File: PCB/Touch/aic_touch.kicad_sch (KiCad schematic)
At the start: 14 parts, among them J1 Antenna, J2 PN5180, J3 PN532, J4 Display, U1 Pico

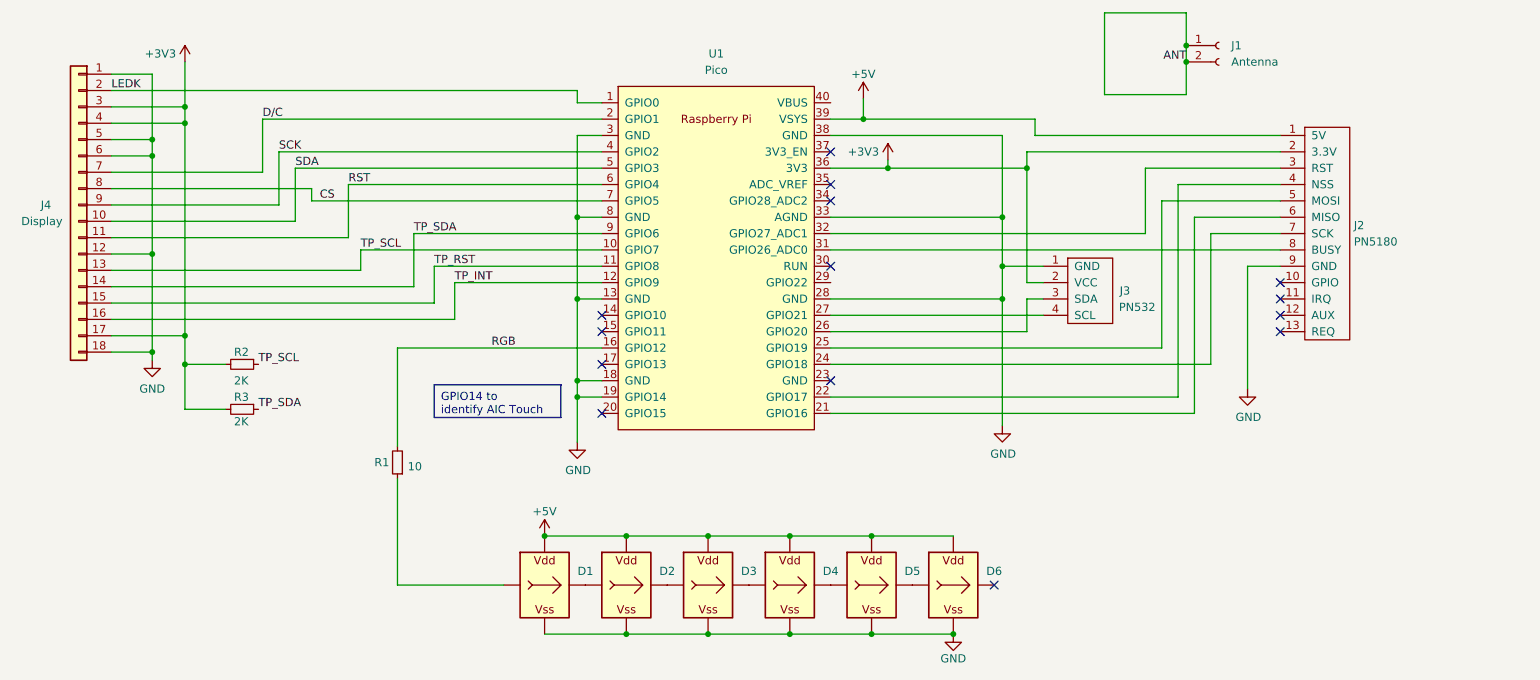
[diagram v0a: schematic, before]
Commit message: Fix PCB issue and change to 4020 RGB
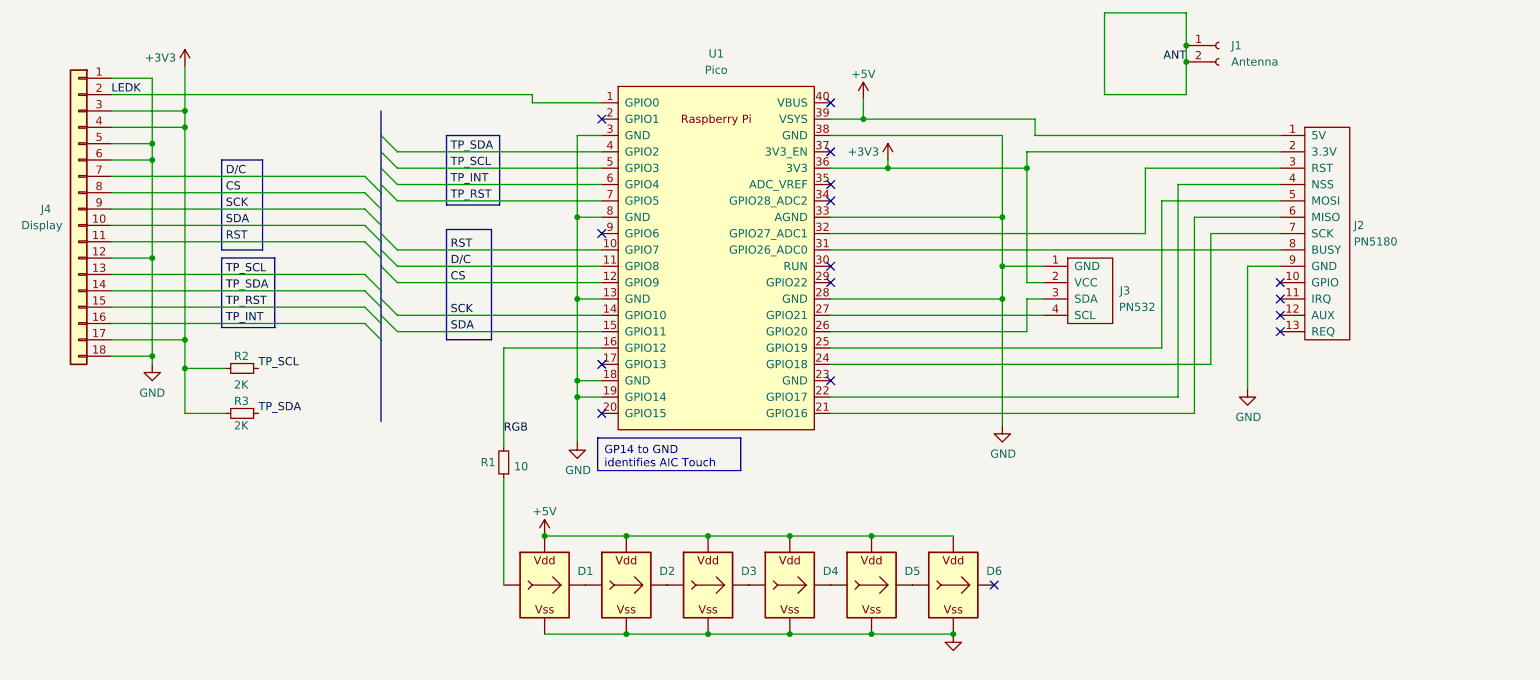
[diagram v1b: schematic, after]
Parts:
- D1, D2, D3, D4, D5, D6: footprint aic_pico:WS2812B-1204 -> aic_pico:WS2812B-4020
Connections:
- net CS: now also U1.12 (GPIO9); no longer U1.7 (GPIO5)
- net D/C: now also U1.11 (GPIO8); no longer U1.2 (GPIO1)
- net RST: now also U1.10 (GPIO7); no longer U1.6 (GPIO4)
- net SCK: now also U1.14 (GPIO10); no longer U1.4 (GPIO2)
- net SDA: now also U1.15 (GPIO11); no longer U1.5 (GPIO3)
- net TP_INT: now also U1.6 (GPIO4); no longer U1.12 (GPIO9)
- net TP_RST: now also U1.7 (GPIO5); no longer U1.11 (GPIO8)
- net TP_SCL: now also U1.5 (GPIO3); no longer U1.10 (GPIO7)
- net TP_SDA: now also U1.4 (GPIO2); no longer U1.9 (GPIO6)
- no-connect marks 14 -> 16
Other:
- moved on the sheet: J4, R1, R2, R3

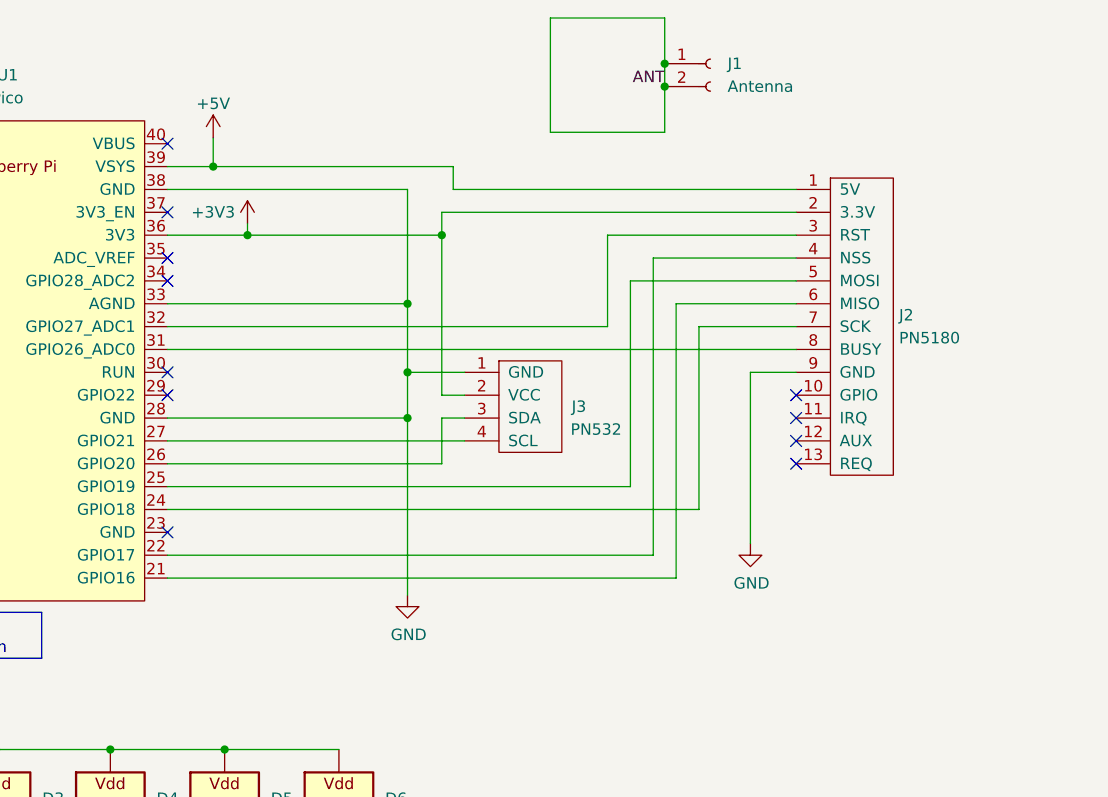
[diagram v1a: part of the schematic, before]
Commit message: Power filtering for PN5180 on AIC touch
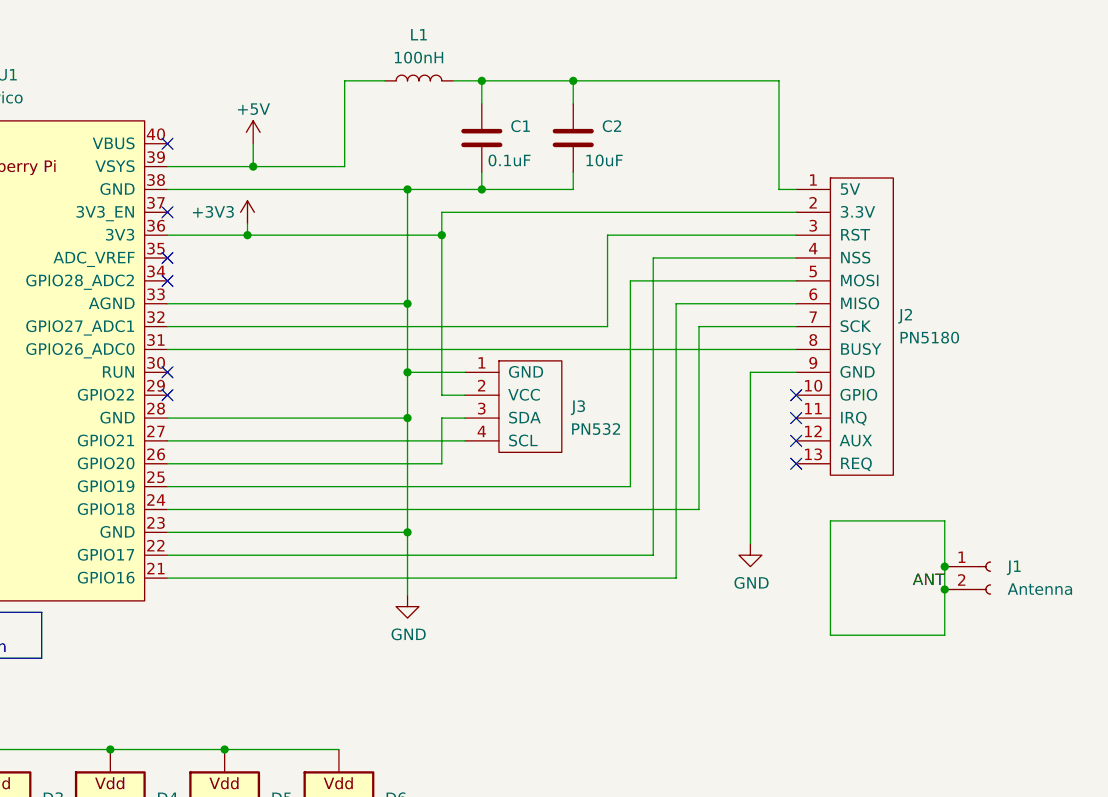
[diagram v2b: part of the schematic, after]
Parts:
- added C1: 0.1uF, Capacitor_SMD:C_0603_1608Metric, symbol Device:C
- added C2: 10uF, Capacitor_SMD:C_0603_1608Metric, symbol Device:C
- added L1: 100nH, Inductor_SMD:L_0805_2012Metric, symbol Device:L
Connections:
- net +5V: now also L1.1; no longer J2.1 (5V)
- net GND: now also U1.23 (GND), C1.2, C2.2
- new net: C1.1, C2.1, J2.1 (5V), L1.2
- no-connect marks 16 -> 15
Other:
- moved on the sheet: J1

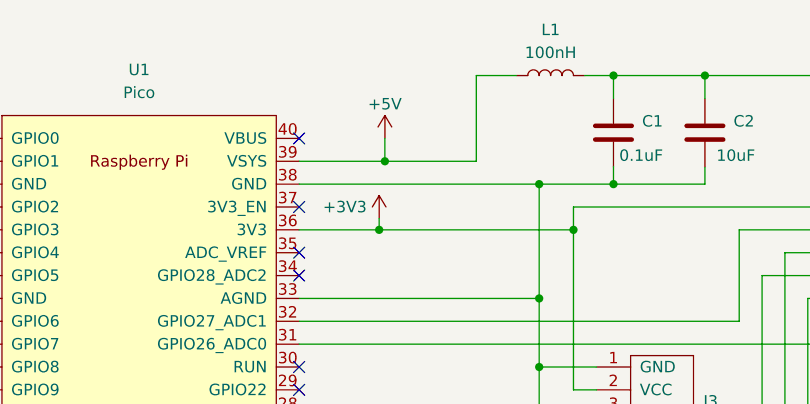
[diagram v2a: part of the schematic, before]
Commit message: L1 to 1206 and power from VBUS
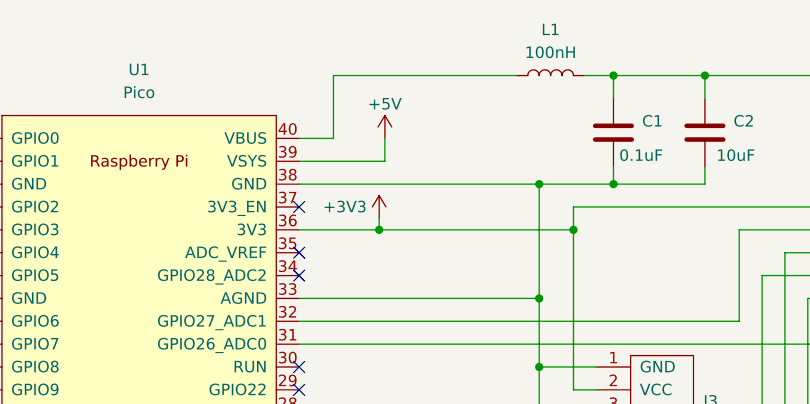
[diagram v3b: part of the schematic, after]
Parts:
- L1: footprint Inductor_SMD:L_0805_2012Metric -> Inductor_SMD:L_1206_3216Metric
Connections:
- net +5V: no longer L1.1
- net at U1.40 (VBUS): now also L1.1
- no-connect marks 15 -> 14
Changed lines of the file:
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@@
   (junction (at 236.22 93.98) (diameter 0) (color 0 0 0 0)
-  )
-  (junction (at 219.075 78.74) (diameter 0) (color 0 0 0 0)
   )
   (junction (at 295.91 125.73) (diameter 0) (color 0 0 0 0)
@@
   (no_connect (at 209.55 91.44))
   (no_connect (at 234.95 151.13))
-  (no_connect (at 209.55 76.2))
   (no_connect (at 173.99 116.84))
   (no_connect (at 279.4 104.14))
@@
     (stroke (width 0) (type default))
   )
+  (wire (pts (xy 213.36 76.2) (xy 213.36 69.215))
+    (stroke (width 0) (type default))
+  )
   (wire (pts (xy 158.75 114.3) (xy 173.99 114.3))
     (stroke (width 0) (type default))
@@
     (stroke (width 0) (type default))
   )
-  (wire (pts (xy 229.235 69.215) (xy 233.68 69.215))
+  (wire (pts (xy 213.36 69.215) (xy 233.68 69.215))
     (stroke (width 0) (type default))
   )
@@
     (stroke (width 0) (type default))
   )
-  (wire (pts (xy 219.075 78.74) (xy 229.235 78.74))
-    (stroke (width 0) (type default))
-  )
   (wire (pts (xy 295.91 123.19) (xy 295.91 125.73))
     (stroke (width 0) (type default))
@@
     (stroke (width 0) (type default))
   )
+  (wire (pts (xy 209.55 76.2) (xy 213.36 76.2))
+    (stroke (width 0) (type default))
+  )
   (wire (pts (xy 177.8 143.51) (xy 190.5 143.51))
     (stroke (width 0) (type default))
@@
   )
   (wire (pts (xy 109.22 77.47) (xy 109.22 70.485))
-    (stroke (width 0) (type default))
-  )
-  (wire (pts (xy 229.235 78.74) (xy 229.235 69.215))
     (stroke (width 0) (type default))
   )
@@
       (effects (font (size 1.27 1.27)))
     )
-    (property "Footprint" "Inductor_SMD:L_0805_2012Metric" (at 237.49 69.215 0)
-      (effects (font (size 1.27 1.27)) hide)
-    )
+    (property "Footprint" "Inductor_SMD:L_1206_3216Metric" (at 237.49 69.215 0)
+      (effects (font (size 1.27 1.27)) hide)
+    )

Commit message: Hybrid AIC Key PCB and AIC touch RGB back to 1204
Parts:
- removed L1: 100nH, Inductor_SMD:L_1206_3216Metric, symbol Device:L
- added C3: 0.1uF, Capacitor_SMD:C_0603_1608Metric, symbol Device:C
- C2: value 10uF -> 0.1uF
- D1, D2, D3, D4, D5, D6: footprint aic_pico:WS2812B-4020 -> aic_pico:WS2812B-1204
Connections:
- net +3V3: now also C2.1, C3.1
- net +5V: now also C1.1, J2.1 (5V)
- net GND: now also C3.2
- no-connect marks 14 -> 15
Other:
- moved on the sheet: C1

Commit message: Touch PCB v1.4 (may improve RF)
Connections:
- net GND: no longer J2.9 (GND), J3.1 (GND), U1.13 (GND), U1.18 (GND), U1.19 (GPIO14), U1.23 (GND), U1.28 (GND), U1.3 (GND), U1.33 (AGND), U1.8 (GND)
- new net: U1.18 (GND), U1.19 (GPIO14)
- new net 5180_GND: J2.9 (GND), U1.33 (AGND)
- new net 532_GND: J3.1 (GND), U1.13 (GND)
- no-connect marks 15 -> 18
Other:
- moved on the sheet: J2

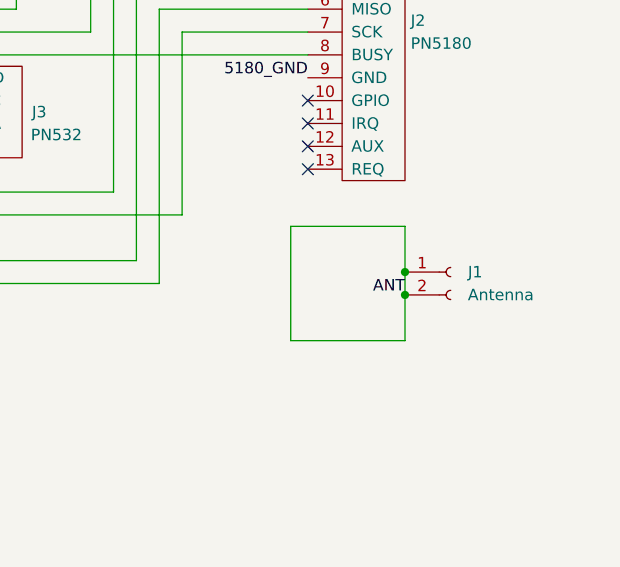
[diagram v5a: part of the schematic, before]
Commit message: Offload PN532 antenna for better signal
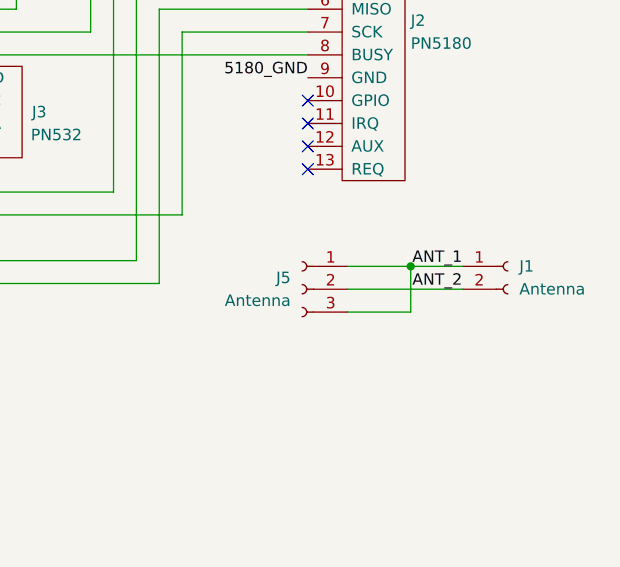
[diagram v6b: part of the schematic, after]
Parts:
- added J5: Antenna, aic_pico:ANT_3P, symbol Connector:Conn_01x03_Socket
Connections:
- net ANT renamed ANT_1
- net ANT_1: now also J5.1 (Pin_1), J5.3 (Pin_3); no longer J1.2 (Pin_2)
- new net ANT_2: J1.2 (Pin_2), J5.2 (Pin_2)
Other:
- moved on the sheet: J1
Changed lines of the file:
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@@
   (junction (at 190.5 158.75) (diameter 0) (color 0 0 0 0)
   )
+  (junction (at 296.545 122.555) (diameter 0) (color 0 0 0 0)
+  )
   (junction (at 177.8 143.51) (diameter 0) (color 0 0 0 0)
   )
@@
   (junction (at 109.22 77.47) (diameter 0) (color 0 0 0 0)
   )
-  (junction (at 295.91 123.19) (diameter 0) (color 0 0 0 0)
-  )
   (junction (at 104.14 100.33) (diameter 0) (color 0 0 0 0)
   )
@@
   )
   (junction (at 242.57 83.82) (diameter 0) (color 0 0 0 0)
-  )
-  (junction (at 295.91 125.73) (diameter 0) (color 0 0 0 0)
   )
   (junction (at 104.14 82.55) (diameter 0) (color 0 0 0 0)
@@
     (stroke (width 0) (type default))
   )
-  (wire (pts (xy 283.21 130.81) (xy 295.91 130.81))
-    (stroke (width 0) (type default))
-  )
   (wire (pts (xy 109.22 117.475) (xy 109.22 113.03))
     (stroke (width 0) (type default))
@@
     (stroke (width 0) (type default))
   )
+  (wire (pts (xy 289.56 125.095) (xy 302.26 125.095))
+    (stroke (width 0) (type default))
+  )
   (wire (pts (xy 170.815 121.92) (xy 173.99 121.92))
     (stroke (width 0) (type default))
@@
     (stroke (width 0) (type default))
   )
+  (wire (pts (xy 296.545 122.555) (xy 289.56 122.555))
+    (stroke (width 0) (type default))
+  )
   (wire (pts (xy 190.5 158.75) (xy 203.2 158.75))
     (stroke (width 0) (type default))
@@
     (stroke (width 0) (type default))
   )
+  (wire (pts (xy 296.545 122.555) (xy 296.545 127.635))
+    (stroke (width 0) (type default))
+  )
   (wire (pts (xy 97.79 102.87) (xy 137.16 102.87))
     (stroke (width 0) (type default))
@@
     (stroke (width 0) (type default))
   )
-  (wire (pts (xy 295.91 123.19) (xy 295.91 125.73))
-    (stroke (width 0) (type default))
-  )
   (wire (pts (xy 218.44 85.09) (xy 218.44 86.36))
     (stroke (width 0) (type default))
@@
     (stroke (width 0) (type default))
   )
-  (wire (pts (xy 295.91 130.81) (xy 295.91 125.73))
-    (stroke (width 0) (type default))
-  )
   (wire (pts (xy 177.8 143.51) (xy 190.5 143.51))
     (stroke (width 0) (type default))
@@
     (stroke (width 0) (type default))
   )
-  (wire (pts (xy 295.91 123.19) (xy 295.91 118.11))
-    (stroke (width 0) (type default))
-  )
   (wire (pts (xy 158.75 134.62) (xy 158.75 151.13))
     (stroke (width 0) (type default))
@@
     (stroke (width 0) (type default))
   )
+  (wire (pts (xy 296.545 127.635) (xy 289.56 127.635))
+    (stroke (width 0) (type default))
+  )
   (wire (pts (xy 227.33 93.98) (xy 242.57 93.98))
     (stroke (width 0) (type default))
@@
     (stroke (width 0) (type default))
   )
-  (wire (pts (xy 295.91 118.11) (xy 283.21 118.11))
+  (wire (pts (xy 302.26 122.555) (xy 296.545 122.555))
     (stroke (width 0) (type default))
   )
@@
   )
   (bus (pts (xy 139.7 107.95) (xy 139.7 109.22))
-    (stroke (width 0) (type default))
-  )
-  (wire (pts (xy 283.21 118.11) (xy 283.21 130.81))
     (stroke (width 0) (type default))
   )
@@
     (effects (font (size 1.27 1.27)) (justify left bottom))
   )
+  (label "ANT_2" (at 302.26 125.095 180) (fields_autoplaced)
+    (effects (font (size 1.27 1.27)) (justify right bottom))
+  )
   (label "SCK" (at 150.495 109.22 0) (fields_autoplaced)
     (effects (font (size 1.27 1.27)) (justify left bottom))
@@
     (effects (font (size 1.27 1.27)) (justify left bottom))
   )
-  (label "ANT" (at 295.91 125.73 180) (fields_autoplaced)
+  (label "ANT_1" (at 302.26 122.555 180) (fields_autoplaced)
     (effects (font (size 1.27 1.27)) (justify right bottom))
   )
@@
         (path "/2e3f5573-c264-4a8b-a2f0-0e6473d39aad"
           (reference "J4") (unit 1)
+        )
+      )
+    )
+  )
+  (symbol (lib_id "Connector:Conn_01x03_Socket") (at 284.48 125.095 0) (mirror y) (unit 1)
+    (in_bom yes) (on_board yes) (dnp no)
+    (property "Reference" "J5" (at 283.21 123.825 0)
+      (effects (font (size 1.27 1.27)) (justify left))
+    )
+    (property "Value" "Antenna" (at 283.21 126.365 0)
+      (effects (font (size 1.27 1.27)) (justify left))
+    )
+    (property "Footprint" "aic_pico:ANT_3P" (at 284.48 125.095 0)
+      (effects (font (size 1.27 1.27)) hide)
+    )
+    (property "Datasheet" "~" (at 284.48 125.095 0)
+      (effects (font (size 1.27 1.27)) hide)
+    )
+    (pin "1")
+    (pin "2")
+    (pin "3")
+    (instances
+      (project "aic_touch"
+        (path "/2e3f5573-c264-4a8b-a2f0-0e6473d39aad"
+          (reference "J5") (unit 1)
         )
       )
@@
     )
   )
-  (symbol (lib_id "Connector:Conn_01x02_Female") (at 300.99 123.19 0) (unit 1)
+  (symbol (lib_id "Connector:Conn_01x02_Female") (at 307.34 122.555 0) (unit 1)
     (in_bom yes) (on_board yes) (dnp no) (fields_autoplaced)
-    (property "Reference" "J1" (at 302.895 123.19 0)
+    (property "Reference" "J1" (at 308.61 122.555 0)
       (effects (font (size 1.27 1.27)) (justify left))
     )
-    (property "Value" "Antenna" (at 302.895 125.73 0)
+    (property "Value" "Antenna" (at 308.61 125.095 0)
       (effects (font (size 1.27 1.27)) (justify left))
     )
-    (property "Footprint" "aic_pico:ANT_2P" (at 300.99 123.19 0)
-      (effects (font (size 1.27 1.27)) hide)
-    )
-    (property "Datasheet" "~" (at 300.99 123.19 0)
-      (effects (font (size 1.27 1.27)) hide)
-    )
+    (property "Footprint" "aic_pico:ANT_2P" (at 307.34 122.555 0)
+      (effects (font (size 1.27 1.27)) hide)
+    )
+    (property "Datasheet" "~" (at 307.34 122.555 0)
+      (effects (font (size 1.27 1.27)) hide)
+    )
